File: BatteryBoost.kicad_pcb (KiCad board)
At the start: 2 copper layers, 80 x 40 mm, 44 parts, among them J1 Mounting Hole, J2 Mounting Hole, J3 Mounting Hole, J4 Mounting Hole, J5 USB_B_Micro, J6 Battery, J7 Output, Q1 -40V 7.5A 2.5V @ 250uA 40mΩ @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, Q2 -40V 7.5A 40mΩ @ 6A, Q4 20V 7.5A 24mΩ @ 2.5Vgs, SW1 SW_SPDT, U1 SP34063AEN, U2 TP4056, U3 AP9101CK6

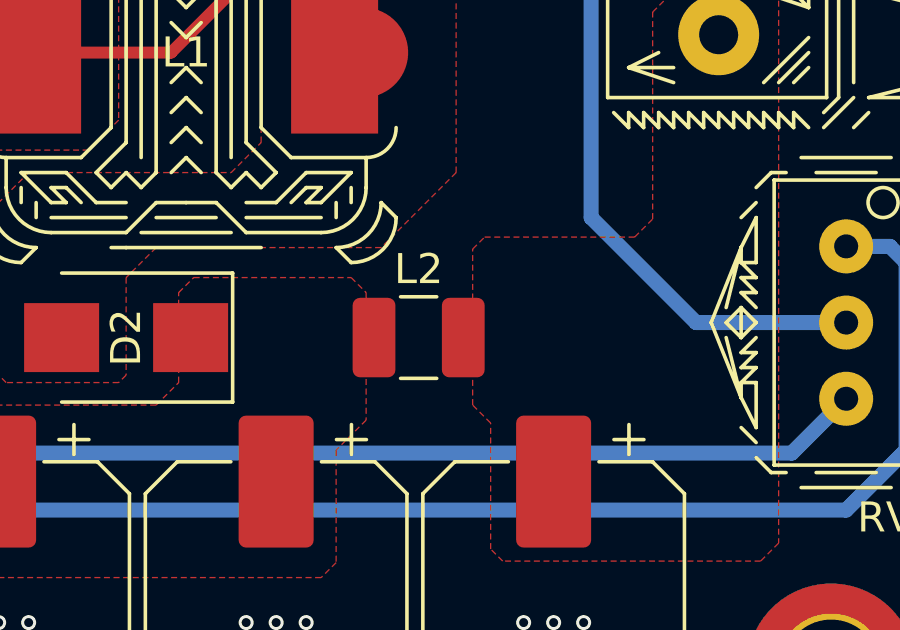
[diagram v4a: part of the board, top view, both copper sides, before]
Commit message: Add new filter inductor footprint
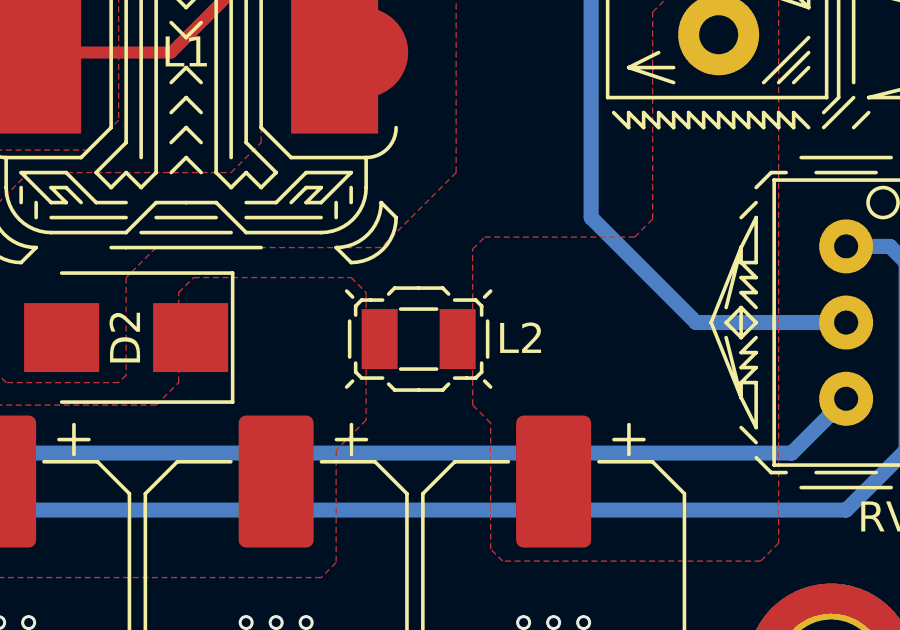
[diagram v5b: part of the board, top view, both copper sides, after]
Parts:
- L2: footprint Inductor_SMD:L_1210_3225Metric_Pad1.42x2.65mm_HandSolder -> BatteryBoost:L_2.5x2.0_Hand_Solder
- moved L2 0.05 mm to (62.0, 24.8)
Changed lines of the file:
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@@
     (add_net VBATT)
   )
-  (module Inductor_SMD:L_1210_3225Metric_Pad1.42x2.65mm_HandSolder (layer F.Cu)
-    (at 62 24.75)
-    (descr "Inductor SMD 1210 (3225 Metric), square (rectangular) end terminal, IPC_7351 nominal with elongated pad for handsoldering. (Body size source: http://www.tortai-tech.com/upload/download/2011102023233369053.pdf), generated with kicad-footprint-generator")
-    (tags "inductor handsolder")
-    (attr smd)
-    (fp_text reference L2 (at 0 -2.28) (layer F.SilkS)
+  (module BatteryBoost:L_2.5x2.0_Hand_Solder (layer F.Cu)
+    (at 62 24.8)
+    (fp_text reference L2 (at 3.4 0) (layer F.SilkS)
       (effects (font (size 1 1) (thickness 0.15)))
     )
-    (fp_text value "1uH ±20% 3.29A 59mΩ" (at 0 2.28) (layer F.Fab)
+    (fp_text value "1uH ±20% 3.29A 59mΩ" (at 0 5.08) (layer F.Fab)
       (effects (font (size 1 1) (thickness 0.15)))
     )
-    (fp_text user %R (at 0 0) (layer F.Fab)
-      (effects (font (size 0.8 0.8) (thickness 0.12)))
-    )
-    (fp_line (start -1.6 1.25) (end -1.6 -1.25) (layer F.Fab) (width 0.1))
-    (fp_line (start -1.6 -1.25) (end 1.6 -1.25) (layer F.Fab) (width 0.1))
-    (fp_line (start 1.6 -1.25) (end 1.6 1.25) (layer F.Fab) (width 0.1))
-    (fp_line (start 1.6 1.25) (end -1.6 1.25) (layer F.Fab) (width 0.1))
-    (fp_line (start -0.602064 -1.36) (end 0.602064 -1.36) (layer F.SilkS) (width 0.12))
-    (fp_line (start -0.602064 1.36) (end 0.602064 1.36) (layer F.SilkS) (width 0.12))
-    (fp_line (start -2.45 1.58) (end -2.45 -1.58) (layer F.CrtYd) (width 0.05))
-    (fp_line (start -2.45 -1.58) (end 2.45 -1.58) (layer F.CrtYd) (width 0.05))
-    (fp_line (start 2.45 -1.58) (end 2.45 1.58) (layer F.CrtYd) (width 0.05))
-    (fp_line (start 2.45 1.58) (end -2.45 1.58) (layer F.CrtYd) (width 0.05))
-    (pad 2 smd roundrect (at 1.4875 0) (size 1.425 2.65) (layers F.Cu F.Paste F.Mask) (roundrect_rratio 0.175439)
+    (fp_line (start 0.6 -1) (end -0.6 -1) (layer F.SilkS) (width 0.12))
+    (fp_line (start -0.6 1) (end 0.6 1) (layer F.SilkS) (width 0.12))
+    (fp_line (start -2.1 -0.8) (end -2.1 -1.1) (layer F.SilkS) (width 0.12))
+    (fp_line (start -2.1 -1.1) (end -1.9 -1.3) (layer F.SilkS) (width 0.12))
+    (fp_line (start -1.9 -1.3) (end -1.6 -1.3) (layer F.SilkS) (width 0.12))
+    (fp_line (start -1.6 -1.3) (end -1.2 -1.3) (layer F.SilkS) (width 0.12))
+    (fp_line (start 1.6 1.3) (end 1.2 1.3) (layer F.SilkS) (width 0.12))
+    (fp_line (start 2.1 0.8) (end 2.1 1.1) (layer F.SilkS) (width 0.12))
+    (fp_line (start 2.1 1.1) (end 1.9 1.3) (layer F.SilkS) (width 0.12))
+    (fp_line (start 1.9 1.3) (end 1.6 1.3) (layer F.SilkS) (width 0.12))
+    (fp_line (start 1.2 -1.3) (end 1.9 -1.3) (layer F.SilkS) (width 0.12))
+    (fp_line (start 1.9 -1.3) (end 2.1 -1.1) (layer F.SilkS) (width 0.12))
+    (fp_line (start 2.1 -1.1) (end 2.1 -0.8) (layer F.SilkS) (width 0.12))
+    (fp_line (start -2.1 1.1) (end -2.1 0.8) (layer F.SilkS) (width 0.12))
+    (fp_line (start -1.9 1.3) (end -2.1 1.1) (layer F.SilkS) (width 0.12))
+    (fp_line (start -1.2 1.3) (end -1.9 1.3) (layer F.SilkS) (width 0.12))
+    (fp_line (start -2.3 -0.6) (end -2.3 0.6) (layer F.SilkS) (width 0.12))
+    (fp_line (start 2.3 -0.6) (end 2.3 0.6) (layer F.SilkS) (width 0.12))
+    (fp_line (start -2.2 -1.4) (end -2.4 -1.6) (layer F.SilkS) (width 0.12))
+    (fp_line (start 2.2 -1.4) (end 2.4 -1.6) (layer F.SilkS) (width 0.12))
+    (fp_line (start 2.2 1.4) (end 2.4 1.6) (layer F.SilkS) (width 0.12))
+    (fp_line (start -2.2 1.4) (end -2.4 1.6) (layer F.SilkS) (width 0.12))
+    (fp_line (start -1 -1.5) (end -0.8 -1.7) (layer F.SilkS) (width 0.12))
+    (fp_line (start -0.8 -1.7) (end 0 -1.7) (layer F.SilkS) (width 0.12))
+    (fp_line (start 0.8 -1.7) (end 0 -1.7) (layer F.SilkS) (width 0.12))
+    (fp_line (start 0.8 -1.7) (end 1 -1.5) (layer F.SilkS) (width 0.12))
+    (fp_line (start 1 1.5) (end 0.8 1.7) (layer F.SilkS) (width 0.12))
+    (fp_line (start 0.8 1.7) (end 0 1.7) (layer F.SilkS) (width 0.12))
+    (fp_line (start -0.8 1.7) (end 0 1.7) (layer F.SilkS) (width 0.12))
+    (fp_line (start -0.8 1.7) (end -1 1.5) (layer F.SilkS) (width 0.12))
+    (fp_line (start -1.25 -1) (end 1.25 -1) (layer F.CrtYd) (width 0.12))
+    (fp_line (start 1.25 -1) (end 1.25 1) (layer F.CrtYd) (width 0.12))
+    (fp_line (start 1.25 1) (end -1.25 1) (layer F.CrtYd) (width 0.12))
+    (fp_line (start -1.25 1) (end -1.25 -1) (layer F.CrtYd) (width 0.12))
+    (pad 2 smd rect (at 1.3 0 180) (size 1.2 2) (layers F.Cu F.Paste F.Mask)
       (net 21 /Vout))
-    (pad 1 smd roundrect (at -1.4875 0) (size 1.425 2.65) (layers F.Cu F.Paste F.Mask) (roundrect_rratio 0.175439)
+    (pad 1 smd rect (at -1.3 0) (size 1.2 2) (layers F.Cu F.Paste F.Mask)
       (net 20 SMPS_Output))
-    (model ${KISYS3DMOD}/Inductor_SMD.3dshapes/L_1210_3225Metric.wrl
-      (at (xyz 0 0 0))
-      (scale (xyz 1 1 1))
+    (model "U:/My Documents/Git/Personal/BatteryBoost_5V-24V/Libraries/Footprints/BatteryBoost.pretty/STEP Files/Inductor_2520.step"
+      (offset (xyz 0 -1.1 0.5))
+      (scale (xyz 1 1 0.54))
       (rotate (xyz 0 0 0))
     )

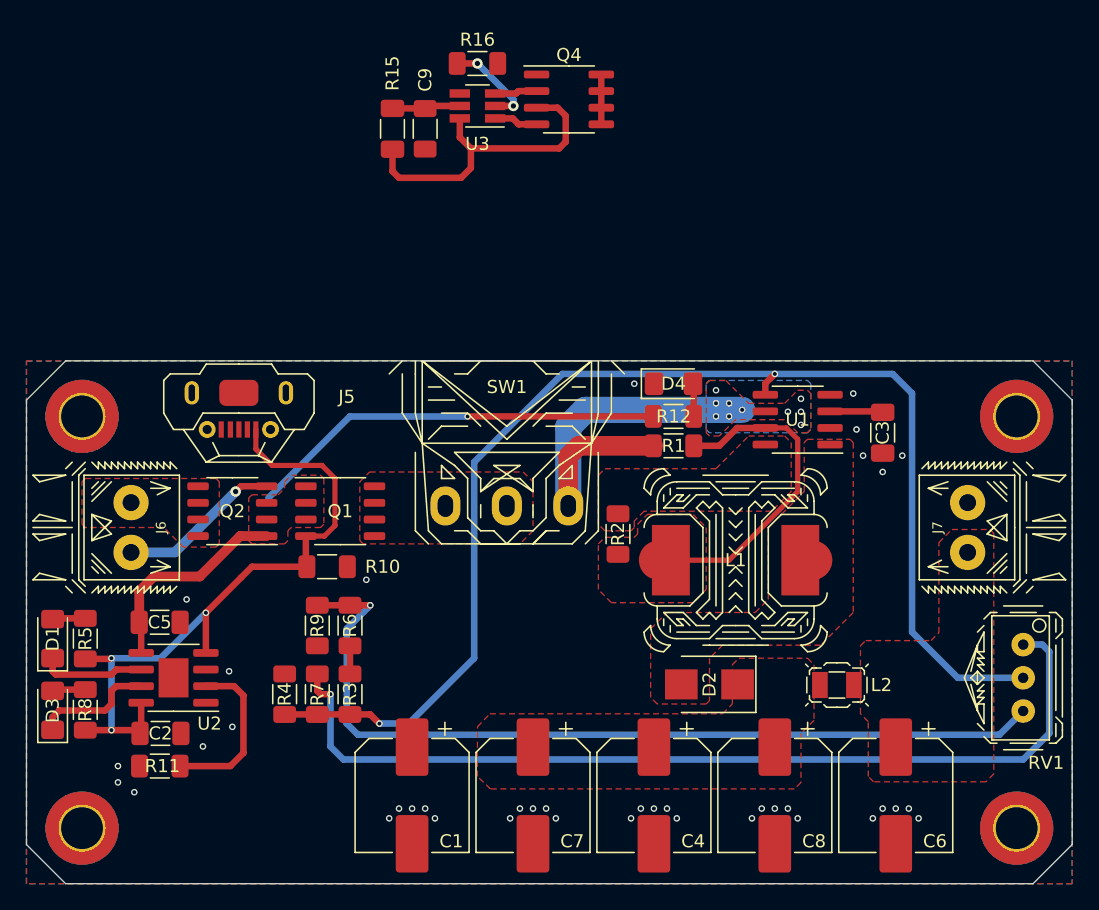
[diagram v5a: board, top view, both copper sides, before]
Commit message: place and route battery protection circuit
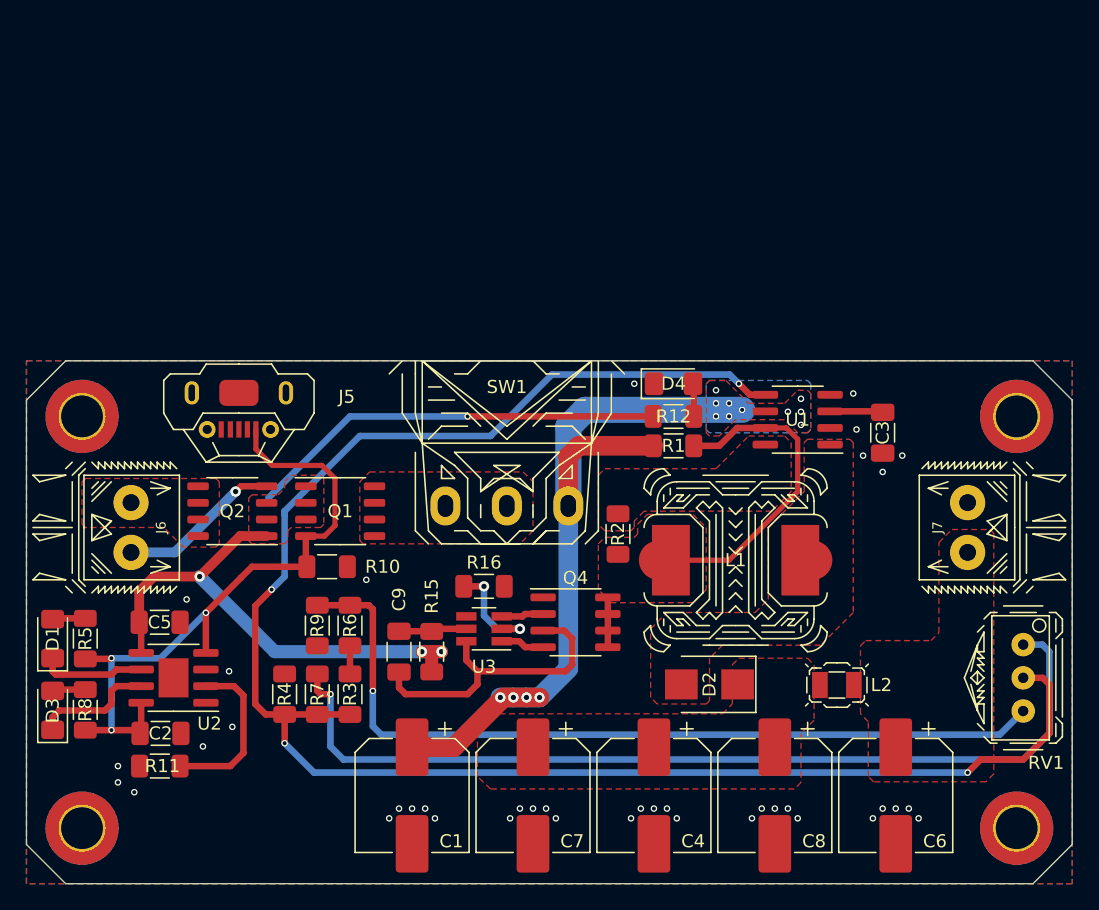
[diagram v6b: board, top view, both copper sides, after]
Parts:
- moved C9 40.0 mm to (28.5, 22.2)
- moved Q4 40.0 mm to (42.0, 20.0)
- moved R15 40.0 mm to (31.0, 22.2)
- moved R16 40.0 mm to (35.0, 17.2)
- moved U3 40.0 mm to (35.0, 20.5)
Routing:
- net SMPS_VoltageSetting: track 98.9 -> 134.1 mm, vias 2 -> 4
- net SMPS_Pwr: track 62.6 -> 92.4 mm, vias 11 -> 15
- net VBATT: track 16.3 -> 40.2 mm, vias 0 -> 3
- net Net-(R6-Pad2): track 66.7 -> 64.1 mm
- net Net-(R16-Pad1): track 7.34 -> 8.36 mm
- net /Raw_Batt_-: track 36.7 -> 35.7 mm

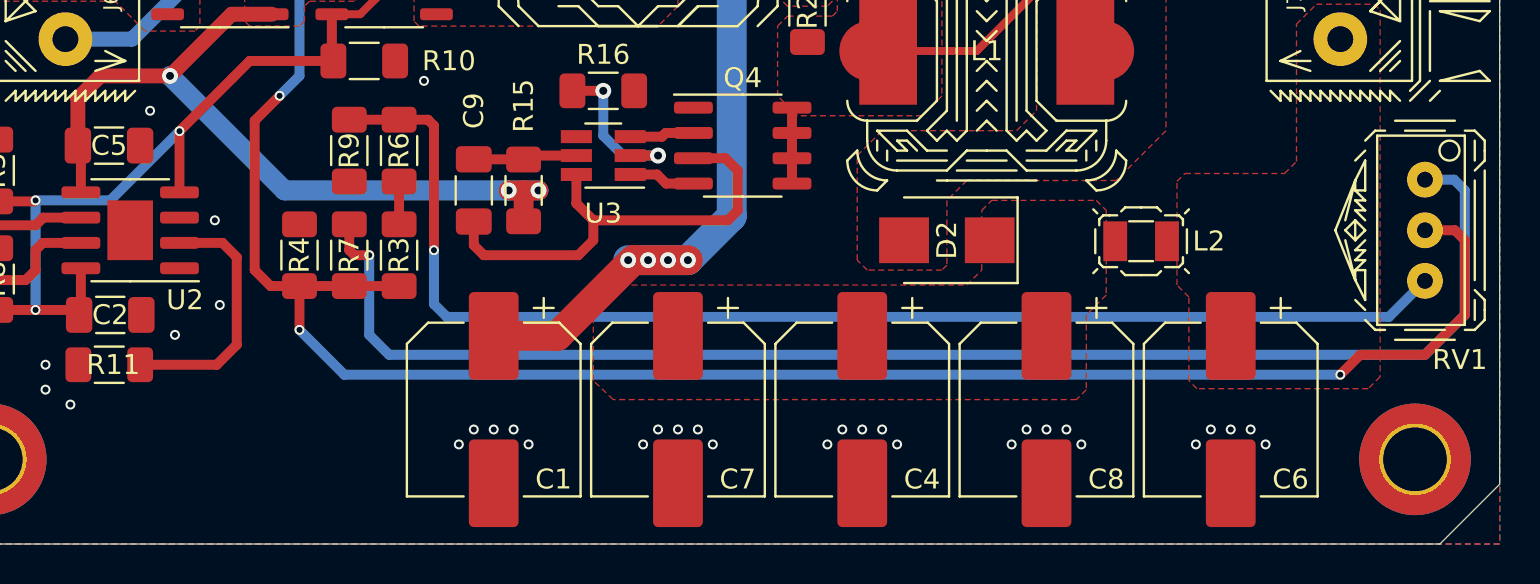
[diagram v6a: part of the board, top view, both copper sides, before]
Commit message: move potentiometer
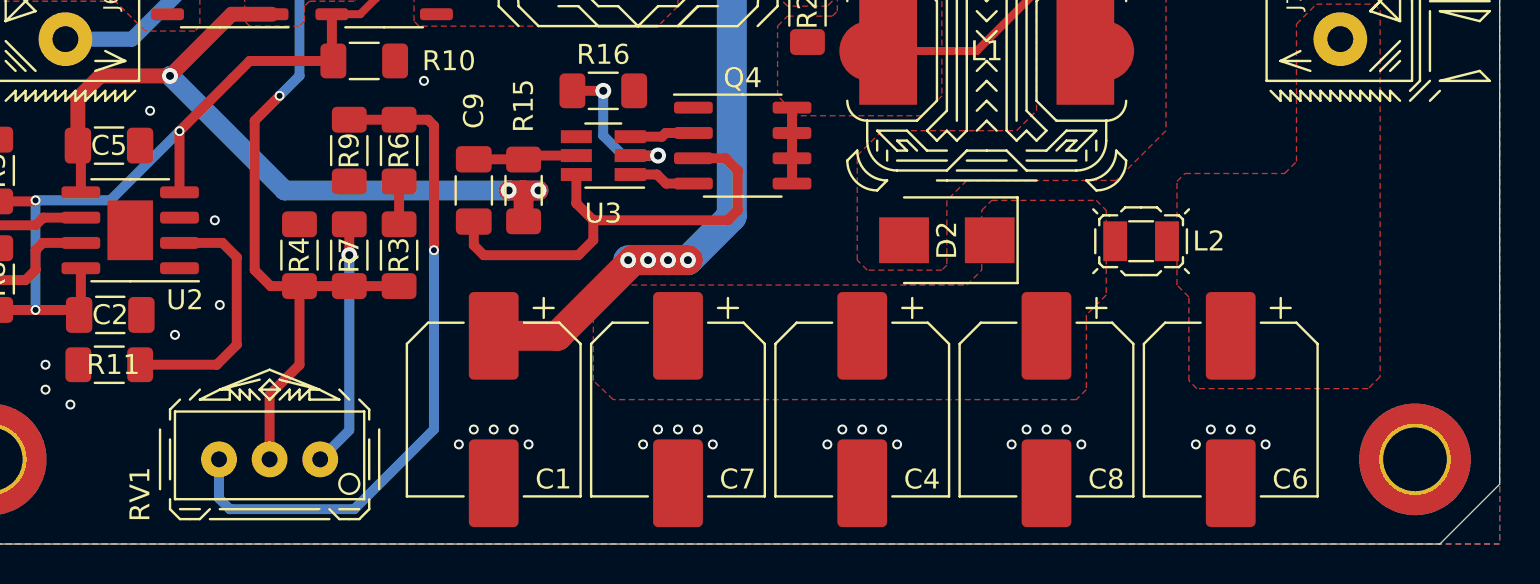
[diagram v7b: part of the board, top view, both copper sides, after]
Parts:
- moved RV1 59.1 mm to (18.2, 35.8), turned to 0 degrees
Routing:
- net SMPS_VoltageSetting: track 134.1 -> 74.6 mm, vias 4 -> 2
- net Net-(R7-Pad1): track 71.1 -> 12.4 mm
- net Net-(R6-Pad2): track 64.1 -> 34.3 mm
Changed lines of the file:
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@@
     (thickness 1.6)
     (drawings 12)
-    (tracks 237)
+    (tracks 223)
     (zones 0)
     (modules 44)
@@
   )
   (setup
-    (last_trace_width 1.5)
+    (last_trace_width 0.5)
     (user_trace_width 0.4)
     (user_trace_width 0.5)
@@
   )
   (module BatteryBoost:Potentiometer_3296W-1-504 (layer F.Cu)
-    (at 76.25 24.25 90)
-    (fp_text reference RV1 (at -6.5 1.75 180) (layer F.SilkS)
+    (at 18.25 35.75)
+    (fp_text reference RV1 (at -6.5 1.75 270) (layer F.SilkS)
       (effects (font (size 1 1) (thickness 0.15)))
     )
-    (fp_text value "Variable Resistors 500kΩ ±10%" (at 0 -6.5 90) (layer F.Fab)
+    (fp_text value "Variable Resistors 500kΩ ±10%" (at 0 -6.5) (layer F.Fab)
       (effects (font (size 1 1) (thickness 0.15)))
     )
@@
     (fp_line (start 0.5 -4) (end 2.5 -3.5) (layer B.SilkS) (width 0.12))
     (fp_circle (center 4 1.23) (end 4 1.73) (layer F.SilkS) (width 0.12))
-    (pad 3 thru_hole circle (at 2.54 0 90) (size 1.8 1.8) (drill 0.8) (layers *.Cu *.Mask)
+    (pad 3 thru_hole circle (at 2.54 0) (size 1.8 1.8) (drill 0.8) (layers *.Cu *.Mask)
       (net 18 "Net-(R7-Pad1)"))
-    (pad 2 thru_hole circle (at 0 0 90) (size 1.8 1.8) (drill 0.8) (layers *.Cu *.Mask)
+    (pad 2 thru_hole circle (at 0 0) (size 1.8 1.8) (drill 0.8) (layers *.Cu *.Mask)
       (net 22 SMPS_VoltageSetting))
-    (pad 1 thru_hole circle (at -2.54 0 90) (size 1.8 1.8) (drill 0.8) (layers *.Cu *.Mask)
+    (pad 1 thru_hole circle (at -2.54 0) (size 1.8 1.8) (drill 0.8) (layers *.Cu *.Mask)
       (net 23 "Net-(R6-Pad2)"))
     (model "${KIPRJMOD}/Libraries/Footprints/BatteryBoost.pretty/STEP Files/bourns3296pot.step"
@@
   (segment (start 8.775 23.615) (end 6.885 23.615) (width 0.5) (layer F.Cu) (net 13))
   (segment (start 24.75 21.8) (end 24.75 23.95) (width 0.5) (layer F.Cu) (net 17))
-  (segment (start 22.25 23.95) (end 22.25 25.25) (width 0.5) (layer F.Cu) (net 18))
-  (segment (start 22.25 25.25) (end 22.5 25.5) (width 0.5) (layer F.Cu) (net 18))
-  (via (at 23.25 25.5) (size 0.5) (drill 0.3) (layers F.Cu B.Cu) (net 18))
-  (segment (start 22.5 25.5) (end 23.25 25.5) (width 0.5) (layer F.Cu) (net 18))
-  (segment (start 77.71 21.71) (end 76.25 21.71) (width 0.5) (layer B.Cu) (net 18))
-  (segment (start 78.25 22.25) (end 77.71 21.71) (width 0.5) (layer B.Cu) (net 18))
-  (segment (start 78.25 28.5) (end 78.25 22.25) (width 0.5) (layer B.Cu) (net 18))
-  (segment (start 76.25 30.5) (end 78.25 28.5) (width 0.5) (layer B.Cu) (net 18))
-  (segment (start 24.25 30.5) (end 76.25 30.5) (width 0.5) (layer B.Cu) (net 18))
-  (segment (start 23.25 29.5) (end 24.25 30.5) (width 0.5) (layer B.Cu) (net 18))
-  (segment (start 23.25 25.5) (end 23.25 29.5) (width 0.5) (layer B.Cu) (net 18))
+  (via (at 22.25 25.5) (size 0.8) (drill 0.4) (layers F.Cu B.Cu) (net 18))
+  (segment (start 22.25 23.95) (end 22.25 25.5) (width 0.5) (layer F.Cu) (net 18))
+  (segment (start 22.25 34.29) (end 20.79 35.75) (width 0.5) (layer B.Cu) (net 18))
+  (segment (start 22.25 25.5) (end 22.25 34.29) (width 0.5) (layer B.Cu) (net 18))
   (segment (start 13.725 24.885) (end 15.885 24.885) (width 0.5) (layer F.Cu) (net 19))
   (segment (start 15.885 24.885) (end 16.6 25.6) (width 0.5) (layer F.Cu) (net 19))
@@
   (segment (start 22.25 27.05) (end 19.75 27.05) (width 0.5) (layer F.Cu) (net 22))
   (segment (start 22.25 27.05) (end 24.75 27.05) (width 0.5) (layer F.Cu) (net 22))
-  (segment (start 76.25 24.25) (end 77.75 24.25) (width 0.5) (layer F.Cu) (net 22))
-  (segment (start 77.75 24.25) (end 78.25 24.75) (width 0.5) (layer F.Cu) (net 22))
-  (segment (start 78.25 24.75) (end 78.25 28.5) (width 0.5) (layer F.Cu) (net 22))
-  (segment (start 78.25 28.5) (end 76.25 30.5) (width 0.5) (layer F.Cu) (net 22))
-  (segment (start 73 30.5) (end 72 31.5) (width 0.5) (layer F.Cu) (net 22))
-  (segment (start 76.25 30.5) (end 73 30.5) (width 0.5) (layer F.Cu) (net 22))
-  (via (at 72 31.5) (size 0.5) (drill 0.3) (layers F.Cu B.Cu) (net 22))
-  (segment (start 72 31.5) (end 22 31.5) (width 0.5) (layer B.Cu) (net 22))
-  (via (at 19.75 29.25) (size 0.5) (drill 0.3) (layers F.Cu B.Cu) (net 22))
-  (segment (start 22 31.5) (end 19.75 29.25) (width 0.5) (layer B.Cu) (net 22))
-  (segment (start 19.75 29.25) (end 19.75 27.05) (width 0.5) (layer F.Cu) (net 22))
   (segment (start 19.75 11.75) (end 19.75 11.5) (width 0.5) (layer B.Cu) (net 22))
   (segment (start 19.75 11.5) (end 25.5 5.75) (width 0.5) (layer B.Cu) (net 22))
@@
   (segment (start 18.3 27.05) (end 17.5 26.25) (width 0.5) (layer F.Cu) (net 22))
   (segment (start 17.5 26.25) (end 17.5 18.75) (width 0.5) (layer F.Cu) (net 22))
+  (segment (start 19.75 27.05) (end 19.75 31) (width 0.5) (layer F.Cu) (net 22))
+  (segment (start 18.25 32.5) (end 18.25 35.75) (width 0.5) (layer F.Cu) (net 22))
+  (segment (start 19.75 31) (end 18.25 32.5) (width 0.5) (layer F.Cu) (net 22))
   (segment (start 24.75 18.7) (end 22.25 18.7) (width 0.5) (layer F.Cu) (net 23))
-  (segment (start 74.439999 28.600001) (end 76.25 26.79) (width 0.5) (layer B.Cu) (net 23))
-  (segment (start 24.75 18.7) (end 26.2 18.7) (width 0.5) (layer F.Cu) (net 23))
-  (segment (start 26.2 18.7) (end 26.5 19) (width 0.5) (layer F.Cu) (net 23))
   (via (at 26.5 25.25) (size 0.5) (drill 0.3) (layers F.Cu B.Cu) (net 23))
   (segment (start 26.5 19) (end 26.5 25.25) (width 0.5) (layer F.Cu) (net 23))
-  (segment (start 26.5 25.25) (end 26.5 27.950002) (width 0.5) (layer B.Cu) (net 23))
-  (segment (start 27.149999 28.600001) (end 74.439999 28.600001) (width 0.5) (layer B.Cu) (net 23))
-  (segment (start 26.5 27.950002) (end 27.149999 28.600001) (width 0.5) (layer B.Cu) (net 23))
+  (segment (start 24.75 18.7) (end 26.2 18.7) (width 0.5) (layer F.Cu) (net 23))
+  (segment (start 26.2 18.7) (end 26.5 19) (width 0.5) (layer F.Cu) (net 23))
+  (segment (start 26.5 34.25) (end 26.5 25.25) (width 0.5) (layer B.Cu) (net 23))
+  (segment (start 22.5 38.25) (end 26.5 34.25) (width 0.5) (layer B.Cu) (net 23))
+  (segment (start 16.25 38.25) (end 22.5 38.25) (width 0.5) (layer B.Cu) (net 23))
+  (segment (start 15.71 37.71) (end 16.25 38.25) (width 0.5) (layer B.Cu) (net 23))
+  (segment (start 15.71 35.75) (end 15.71 37.71) (width 0.5) (layer B.Cu) (net 23))
   (segment (start 39.525 19.365) (end 38.135 19.365) (width 0.5) (layer F.Cu) (net 25))
   (segment (start 37.95 19.55) (end 36.35 19.55) (width 0.5) (layer F.Cu) (net 25))
